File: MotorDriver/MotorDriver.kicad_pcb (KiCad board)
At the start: 2 copper layers, 70 x 70 mm, 95 parts, among them J1 Conn_01x01, J2 Conn_01x01, J3 Conn_01x01, J4 Conn_01x01, J5 Conn_02x05_Odd_Even, J6 Conn_02x03_Odd_Even, J7 4P4C, J8 4P4C, Q1 Q_NMOS_GDS, Q2 Q_NMOS_GDS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

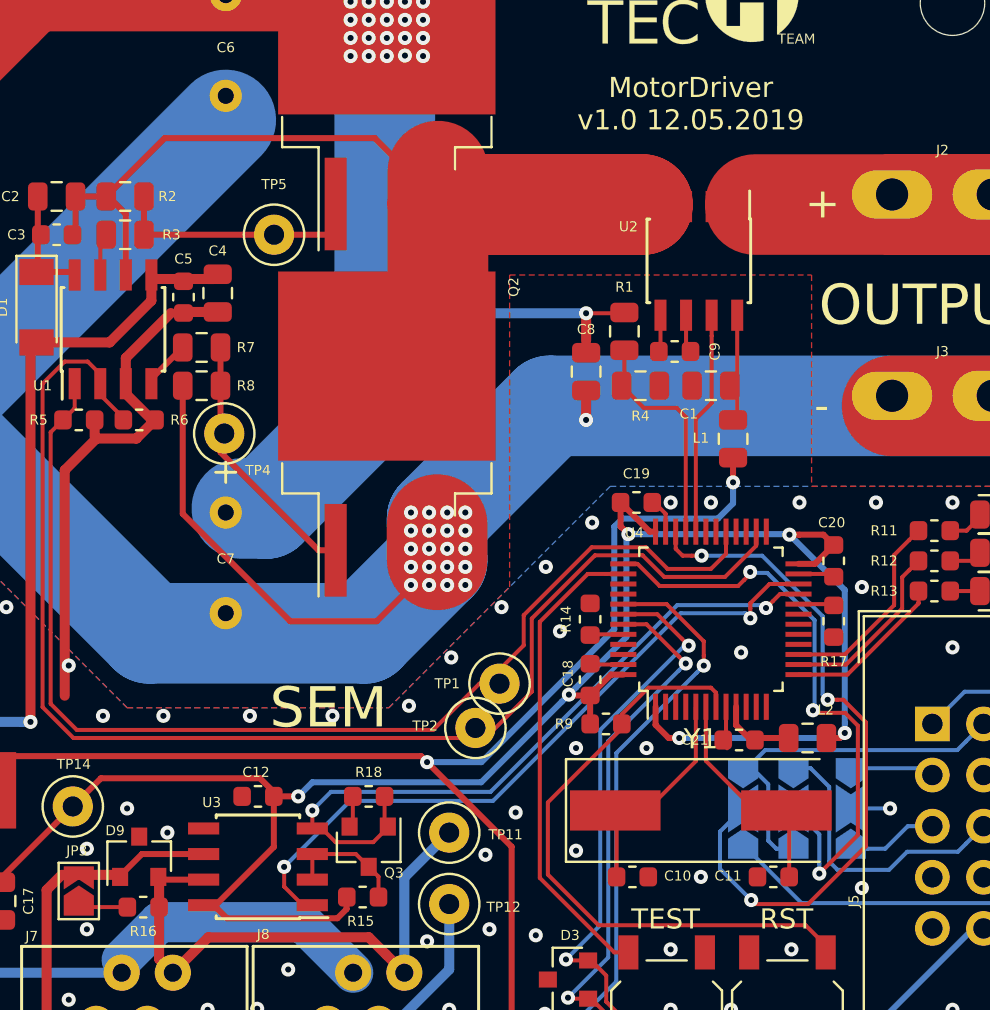
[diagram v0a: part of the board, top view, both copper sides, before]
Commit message: MotorDriver/: Fix known issues
Signed-off-by: Asiderr <norbert.kaminski@3mdeb.com>
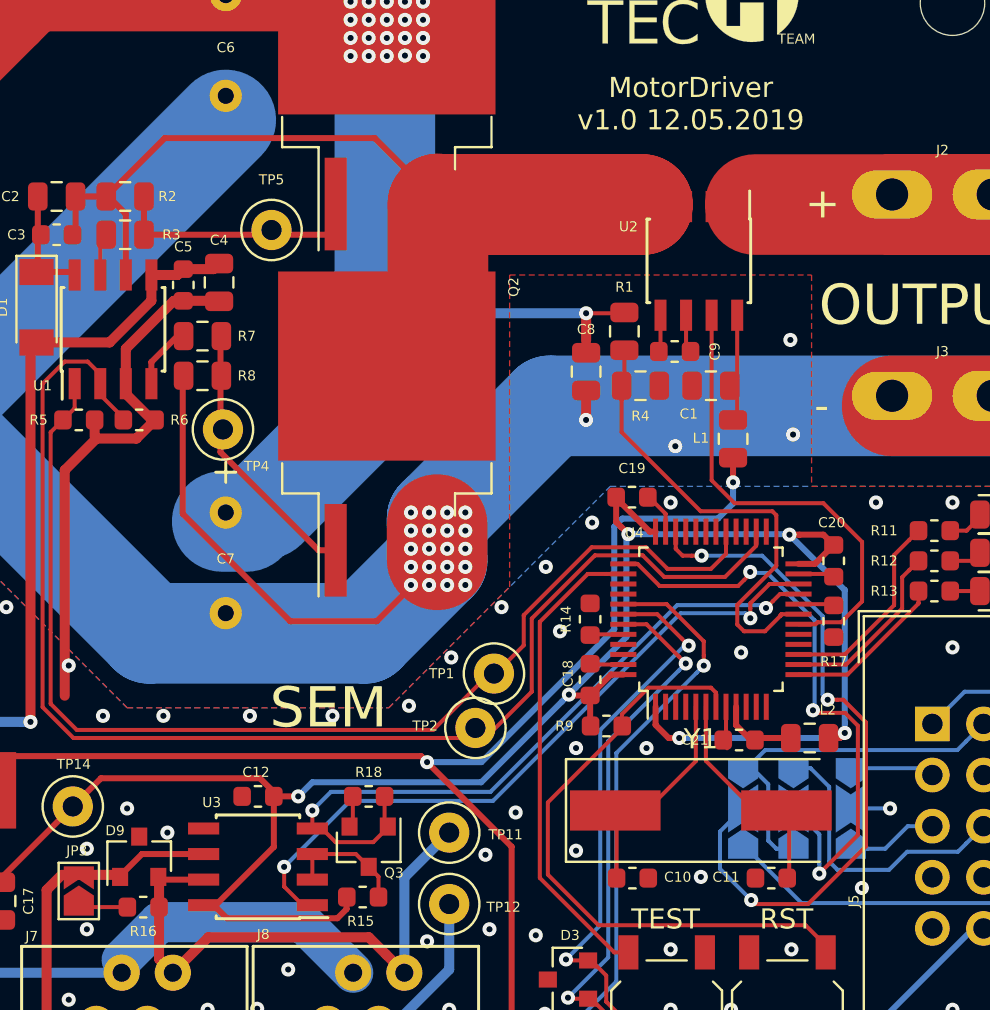
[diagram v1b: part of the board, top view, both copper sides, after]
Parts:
- moved C5 0.60 mm to (126.8, 89.5)
- moved TP1 0.57 mm to (142.2, 108.8)
- moved R7 0.57 mm to (127.7, 92.0)
- moved C4 0.54 mm to (128.6, 89.4)
- moved R8 0.50 mm to (127.7, 94.0)
- moved C19 0.34 mm to (149.1, 100.0)
- moved TP5 0.27 mm to (131.2, 86.8)
- moved TP4 0.21 mm to (128.8, 96.7)
- moved C11 0.12 mm to (156.0, 119.0)
- moved L2 0.11 mm to (157.9, 112.0)
- moved R9 0.11 mm to (147.8, 111.4)
- moved C10 0.06 mm to (149.1, 119.0)
- gave numbers to parts that had none: 1
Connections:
- U4 pad 18: Net-(U4-Pad18) -> /ADC_I
- U4 pad 19: Net-(U4-Pad19) -> /ADC_VIN
- U4 pad 32: /ADC_I -> Net-(U4-Pad32)
- U4 pad 33: /ADC_VIN -> Net-(U4-Pad33)
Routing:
- net /ADC_VIN: track 11.5 -> 24.1 mm
- net /ADC_I: track 11.1 -> 23.6 mm
- net /VS: track 57.1 -> 55.4 mm
- net Net-(R7-Pad2): track 2.65 -> 3.65 mm
- net GND: track 54.1 -> 54.7 mm, vias 79 -> 76
- net Net-(C6-Pad2): vias 21 -> 23
- net (no net): vias 0 -> 1

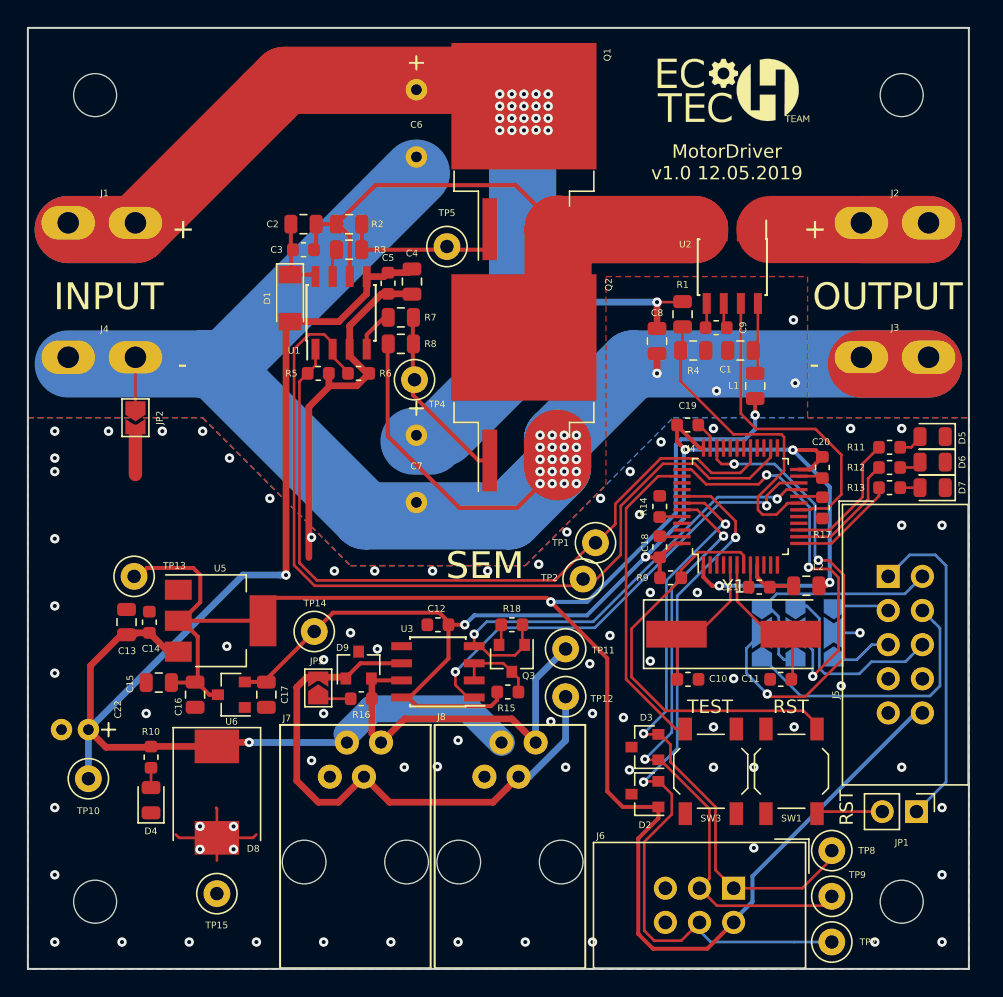
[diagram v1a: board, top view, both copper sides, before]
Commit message: MotorDriver/: Fix pcb layout
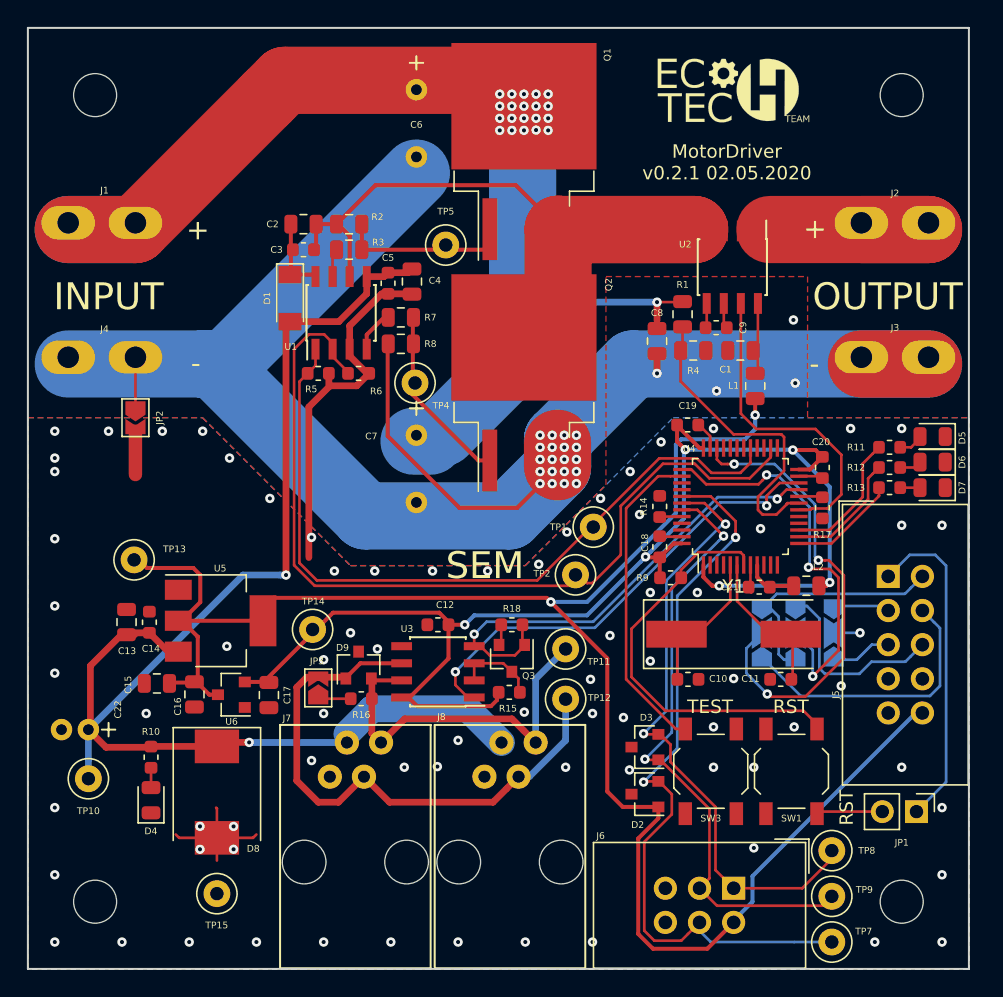
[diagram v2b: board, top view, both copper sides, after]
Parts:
- moved TP13 1.23 mm to (107.9, 110.1)
- moved TP1 1.18 mm to (142.1, 107.6)
- moved TP2 0.65 mm to (140.7, 111.2)
- moved TP4 0.24 mm to (128.8, 96.9)
- moved TP14 0.19 mm to (121.2, 115.3)
- moved C17 0.19 mm to (117.9, 120.1)
- moved TP12 0.18 mm to (140.0, 120.4)
- moved C15 0.16 mm to (109.6, 119.3)
- moved TP5 0.14 mm to (131.1, 86.7)
- moved R15 0.11 mm to (135.8, 119.9)
- moved C16 0.05 mm to (112.4, 120.1)
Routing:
- net /HIN: track 57.4 -> 56.1 mm
- net /LIN: track 66.7 -> 65.9 mm
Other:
- rule via_min_size: 0.7 -> 0.5
- board text added: "MotorDriver v0.2.1 02.05.2020"
- board text removed: "MotorDriver v1.0 12.05.2019"
